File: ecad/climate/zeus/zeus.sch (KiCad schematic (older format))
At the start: 12 parts, among them J1 MCV 1,5/ 2-G-3,5, J10 47053-1000, J11 47053-1000, J12 PT 1,5/4-3,5-H, J13 PT 1,5/4-3,5-H, J2 MCV 1,5/ 2-G-3,5, J3 MCV 1,5/ 2-G-3,5, J5 47053-1000, J6 47053-1000, J7 215079-8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

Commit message: Makes pleiades zeus again
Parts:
- removed J12, J13: PT 1,5/4-3,5-H, TerminalBlock_Phoenix:TerminalBlock_Phoenix_PT-1,5-4-3.5-H_1x04_P3.50mm_Horizontal, symbol Connector_Generic:Conn_01x04
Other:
- moved on the sheet: J3
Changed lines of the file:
@@
 EESchema Schematic File Version 4
-LIBS:pleiades-cache
+LIBS:zeus-cache
 EELAYER 26 0
 EELAYER END
 $Descr A4 11693 8268
 encoding utf-8
-Sheet 1 12
+Sheet 1 10
 Title ""
 Date ""
@@
 L power:+12V #PWR01
 U 1 1 5BA4C0F9
-P 1700 6750
-F 0 "#PWR01" H 1700 6600 50  0001 C CNN
-F 1 "+12V" H 1700 6890 50  0000 C CNN
-F 2 "" H 1700 6750 50  0001 C CNN
-F 3 "" H 1700 6750 50  0001 C CNN
-	1    1700 6750
+P 2200 1250
+F 0 "#PWR01" H 2200 1100 50  0001 C CNN
+F 1 "+12V" H 2200 1390 50  0000 C CNN
+F 2 "" H 2200 1250 50  0001 C CNN
+F 3 "" H 2200 1250 50  0001 C CNN
+	1    2200 1250
 	1    0    0    -1
 $EndComp
@@
 L power:+5V #PWR02
 U 1 1 5BA4C12E
-P 3250 6750
-F 0 "#PWR02" H 3250 6600 50  0001 C CNN
-F 1 "+5V" H 3250 6890 50  0000 C CNN
-F 2 "" H 3250 6750 50  0001 C CNN
-F 3 "" H 3250 6750 50  0001 C CNN
-	1    3250 6750
+P 3750 1250
+F 0 "#PWR02" H 3750 1100 50  0001 C CNN
+F 1 "+5V" H 3750 1390 50  0000 C CNN
+F 2 "" H 3750 1250 50  0001 C CNN
+F 3 "" H 3750 1250 50  0001 C CNN
+	1    3750 1250
 	1    0    0    -1
 $EndComp
@@
 $EndSheet
 $Sheet
-S 3500 6900 1250 200
+S 4000 1400 1250 200
 U 5BA4EFD7
 F0 "3v3 LDO" 60
 F1 "../../common/3V3LDO.sch" 60
-F2 "5V" I L 3500 7000 60
-F3 "3V3" O R 4750 7000 60
-$EndSheet
-$Sheet
-S 1850 6900 1150 200
+F2 "5V" I L 4000 1500 60
+F3 "3V3" O R 5250 1500 60
+$EndSheet
+$Sheet
+S 2350 1400 1150 200
 U 5BA4BC5D
 F0 "5V Buck Converter" 60
 F1 "../../common/12V5VDCDC.sch" 60
-F2 "VIN" I L 1850 7000 60
-F3 "5V" O R 3000 7000 60
+F2 "VIN" I L 2350 1500 60
+F3 "5V" O R 3500 1500 60
 $EndSheet
 $Comp
 L pleiades-rescue:+3.3V #PWR03
 U 1 1 5BA4FC58
-P 4900 6750
-F 0 "#PWR03" H 4900 6600 50  0001 C CNN
-F 1 "+3.3V" H 4900 6890 50  0000 C CNN
-F 2 "" H 4900 6750 50  0001 C CNN
-F 3 "" H 4900 6750 50  0001 C CNN
-	1    4900 6750
+P 5400 1250
+F 0 "#PWR03" H 5400 1100 50  0001 C CNN
+F 1 "+3.3V" H 5400 1390 50  0000 C CNN
+F 2 "" H 5400 1250 50  0001 C CNN
+F 3 "" H 5400 1250 50  0001 C CNN
+	1    5400 1250
 	1    0    0    -1
 $EndComp
@@
 L Connector_Generic:Conn_01x02 J3
 U 1 1 5BA567FD
-P 1050 7000
-F 0 "J3" H 1050 7100 50  0000 C CNN
-F 1 "MCV 1,5/ 2-G-3,5" H 1050 6800 50  0000 C CNN
-F 2 "Connector_Phoenix_MC:PhoenixContact_MCV_1,5_2-G-3.5_1x02_P3.50mm_Vertical" H 1050 7000 50  0001 C CNN
-F 3 "" H 1050 7000 50  0001 C CNN
-F 4 "MCV 1,5/ 2-G-3,5" H 1050 7000 60  0001 C CNN "Part Number"
-	1    1050 7000
+P 1550 1500
+F 0 "J3" H 1550 1600 50  0000 C CNN
+F 1 "MCV 1,5/ 2-G-3,5" H 1550 1300 50  0000 C CNN
+F 2 "Connector_Phoenix_MC:PhoenixContact_MCV_1,5_2-G-3.5_1x02_P3.50mm_Vertical" H 1550 1500 50  0001 C CNN
+F 3 "" H 1550 1500 50  0001 C CNN
+F 4 "MCV 1,5/ 2-G-3,5" H 1550 1500 60  0001 C CNN "Part Number"
+	1    1550 1500
 	-1   0    0    -1
 $EndComp
@@
 L power:GND #PWR08
 U 1 1 5BA570D8
-P 1500 7300
-F 0 "#PWR08" H 1500 7050 50  0001 C CNN
-F 1 "GND" H 1500 7150 50  0000 C CNN
-F 2 "" H 1500 7300 50  0001 C CNN
-F 3 "" H 1500 7300 50  0001 C CNN
-	1    1500 7300
+P 2000 1800
+F 0 "#PWR08" H 2000 1550 50  0001 C CNN
+F 1 "GND" H 2000 1650 50  0000 C CNN
+F 2 "" H 2000 1800 50  0001 C CNN
+F 3 "" H 2000 1800 50  0001 C CNN
+	1    2000 1800
 	1    0    0    -1
 $EndComp
@@
 F7 "SDA_5V" B R 4850 4200 60
 F8 "SCL_5V" O R 4850 4300 60
-F9 "RELAY_1" O R 4850 3500 50
-F10 "RELAY_2" O R 4850 3600 50
 $EndSheet
 $Sheet
@@
 $EndComp
 Wire Wire Line
-	1700 6750 1700 7000
-Wire Wire Line
-	1250 7000 1700 7000
-Wire Wire Line
-	3000 7000 3250 7000
-Wire Wire Line
-	3250 7000 3250 6750
-Connection ~ 3250 7000
-Wire Wire Line
-	4750 7000 4900 7000
-Wire Wire Line
-	4900 7000 4900 6750
+	2200 1250 2200 1500
+Wire Wire Line
+	1750 1500 2200 1500
+Wire Wire Line
+	3500 1500 3750 1500
+Wire Wire Line
+	3750 1500 3750 1250
+Connection ~ 3750 1500
+Wire Wire Line
+	5250 1500 5400 1500
+Wire Wire Line
+	5400 1500 5400 1250
 Wire Wire Line
 	10300 4600 10400 4600
@@
 	1300 4600 900  4600
 Connection ~ 1300 4150
-Connection ~ 1700 7000
-Wire Wire Line
-	1250 7100 1500 7100
-Wire Wire Line
-	1500 7100 1500 7300
+Connection ~ 2200 1500
+Wire Wire Line
+	1750 1600 2000 1600
+Wire Wire Line
+	2000 1600 2000 1800
 Wire Wire Line
 	3400 4050 3600 4050
@@
 	7800 5450 8500 5450
 $Sheet
-S 6100 3650 1250 1250
+S 6100 3550 1250 1300
 U 5BAB6A7C
 F0 "I2C Multiplexer" 60
@@
 F11 "~INT1" I R 7350 4100 60
 F12 "~INT2" I R 7350 4500 60
+F13 "~INT0" I R 7350 3700 50
 $EndSheet
 Wire Wire Line
@@
 	7600 5700 8500 5700
 Wire Wire Line
-	3250 7000 3500 7000
+	3750 1500 4000 1500
 Wire Wire Line
 	10200 4100 10200 4700
@@
 	1300 4150 1550 4150
 Wire Wire Line
-	1700 7000 1850 7000
+	2200 1500 2350 1500
 Wire Wire Line
 	10300 5800 10300 5200
@@
 Wire Wire Line
 	10250 1300 10350 1300
-$Sheet
-S 6100 1100 750  300
-U 5BB4177A
-F0 "Relay 1" 50
-F1 "Relay.sch" 50
-F2 "CMD" I L 6100 1250 50
-F3 "A" B R 6850 1200 50
-F4 "B" B R 6850 1300 50
-$EndSheet
-$Comp
-L Connector_Generic:Conn_01x04 J12
-U 1 1 5BB464E2
-P 7500 1150
-F 0 "J12" H 7579 1142 50  0000 L CNN
-F 1 "PT 1,5/4-3,5-H" H 7579 1051 50  0000 L CNN
-F 2 "TerminalBlock_Phoenix:TerminalBlock_Phoenix_PT-1,5-4-3.5-H_1x04_P3.50mm_Horizontal" H 7500 1150 50  0001 C CNN
-F 3 "~" H 7500 1150 50  0001 C CNN
-F 4 "PT 1,5/4-3,5-H" H 7500 1150 50  0001 C CNN "Part Number"
-	1    7500 1150
-	1    0    0    -1
-$EndComp
-Wire Wire Line
-	7300 1050 7200 1050
-Wire Wire Line
-	7200 1050 7200 1250
-Wire Wire Line
-	7200 1250 7300 1250
-Wire Wire Line
-	6850 1200 7050 1200
-Wire Wire Line
-	7050 1200 7050 1150
-Wire Wire Line
-	7050 1150 7300 1150
-Wire Wire Line
-	6850 1300 7050 1300
-Wire Wire Line
-	7050 1300 7050 1350
-Wire Wire Line
-	7050 1350 7300 1350
-$Sheet
-S 6100 1750 750  300
-U 5BB53554
-F0 "Relay 2" 50
-F1 "Relay.sch" 50
-F2 "CMD" I L 6100 1900 50
-F3 "A" B R 6850 1850 50
-F4 "B" B R 6850 1950 50
-$EndSheet
-$Comp
-L Connector_Generic:Conn_01x04 J13
-U 1 1 5BB5355B
-P 7500 1800
-F 0 "J13" H 7579 1792 50  0000 L CNN
-F 1 "PT 1,5/4-3,5-H" H 7579 1701 50  0000 L CNN
-F 2 "TerminalBlock_Phoenix:TerminalBlock_Phoenix_PT-1,5-4-3.5-H_1x04_P3.50mm_Horizontal" H 7500 1800 50  0001 C CNN
-F 3 "~" H 7500 1800 50  0001 C CNN
-F 4 "PT 1,5/4-3,5-H" H 7500 1800 50  0001 C CNN "Part Number"
-	1    7500 1800
-	1    0    0    -1
-$EndComp
-Wire Wire Line
-	7300 1700 7200 1700
-Wire Wire Line
-	7200 1700 7200 1900
-Wire Wire Line
-	7200 1900 7300 1900
-Wire Wire Line
-	6850 1850 7050 1850
-Wire Wire Line
-	7050 1850 7050 1800
-Wire Wire Line
-	7050 1800 7300 1800
-Wire Wire Line
-	6850 1950 7050 1950
-Wire Wire Line
-	7050 1950 7050 2000
-Wire Wire Line
-	7050 2000 7300 2000
 Wire Wire Line
 	4850 4100 6100 4100
@@
 Wire Wire Line
 	8850 1250 9100 1250
-Wire Wire Line
-	4850 3600 5600 3600
-Wire Wire Line
-	5600 3600 5600 1900
-Wire Wire Line
-	5600 1900 6100 1900
-Wire Wire Line
-	4850 3500 5500 3500
-Wire Wire Line
-	5500 3500 5500 1250
-Wire Wire Line
-	5500 1250 6100 1250
 $EndSCHEMATC

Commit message: Licenses Climate PCB under OHL v1.2
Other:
- note added: "© 2018 Université de Lausanne\n\nThis documentation describes Open Hardware and is licensed under the\nCERN OHL v. 1.2.\n\nYou may redistribute and modify this documentation under the terms of\nthe CERN OHL v.1.2. (http://ohwr.org/cernohl). This documentation is\ndistributed WITHOUT ANY EXPRESS OR IMPLIED WARRANTY,\nINCLUDING OF MERCHANTABILITY, SATISFACTORY QUALITY AND\nFITNESS FOR A PARTICULAR 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"
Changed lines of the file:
@@
 encoding utf-8
 Sheet 1 10
-Title ""
-Date ""
-Rev ""
-Comp ""
-Comment1 ""
-Comment2 ""
+Title "Zeus - Climate Control Board"
+Date "06/11/2018"
+Rev "A"
+Comp "Université de Lausanne"
+Comment1 "Author: Alexandre Tuleu"
+Comment2 "Licensed under the CERN OHL v1.2"
 Comment3 ""
 Comment4 ""
@@
 Wire Wire Line
 	8850 1250 9100 1250
+Text Notes 550  7750 0    50   ~ 0
+© 2018 Université de Lausanne\n\nThis documentation describes Open Hardware and is licensed under the\nCERN OHL v. 1.2.\n\nYou may redistribute and modify this documentation under the terms of\nthe CERN OHL v.1.2. (http://ohwr.org/cernohl). This documentation is\ndistributed WITHOUT ANY EXPRESS OR IMPLIED WARRANTY,\nINCLUDING OF MERCHANTABILITY, SATISFACTORY QUALITY AND\nFITNESS FOR A PARTICULAR PURPOSE. Please see the CERN OHL v.1.2\nfor applicable conditions
 $EndSCHEMATC

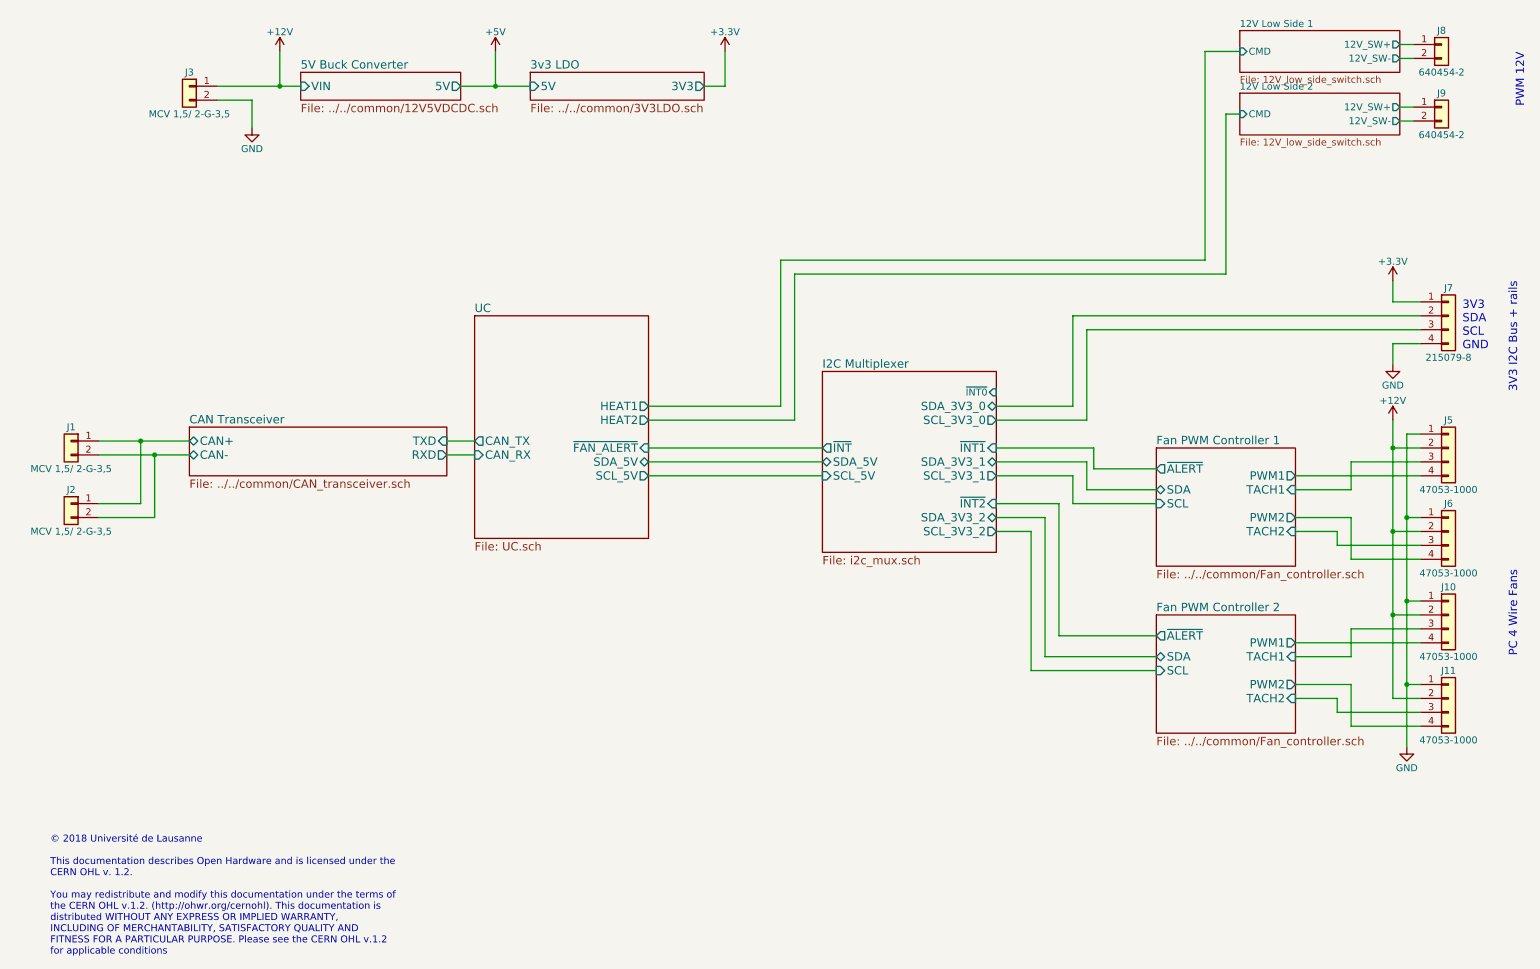
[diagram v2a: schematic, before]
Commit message: Updates climate board to rev B~dev
 * Changes all Power Connectors to MiniFit-JR 5566-02A to avoid
   someone pluging the power supply on the CAN bus as it will destroy
   all MCP2561 on the bus
 * Fixes issues in Arke:
 ** Crossed Rx/Tx lines
 ** Flipped DB9 connector
 * Fixes and Improvment in Celaeno/Zeus:
 ** Added missing pull-up resistor on tachometer inputs
 ** Removed unecessary 32.268kHz oscillators (they are not working
    properly with manual soldering)
 ** Removed I2C multiplexer as we can add a second EMC2302 with a
   different i2c address to do the same thing. Repaced it by an i2c
   level shifter (tested and working).

Many of these changes still need to be tested before going to
production
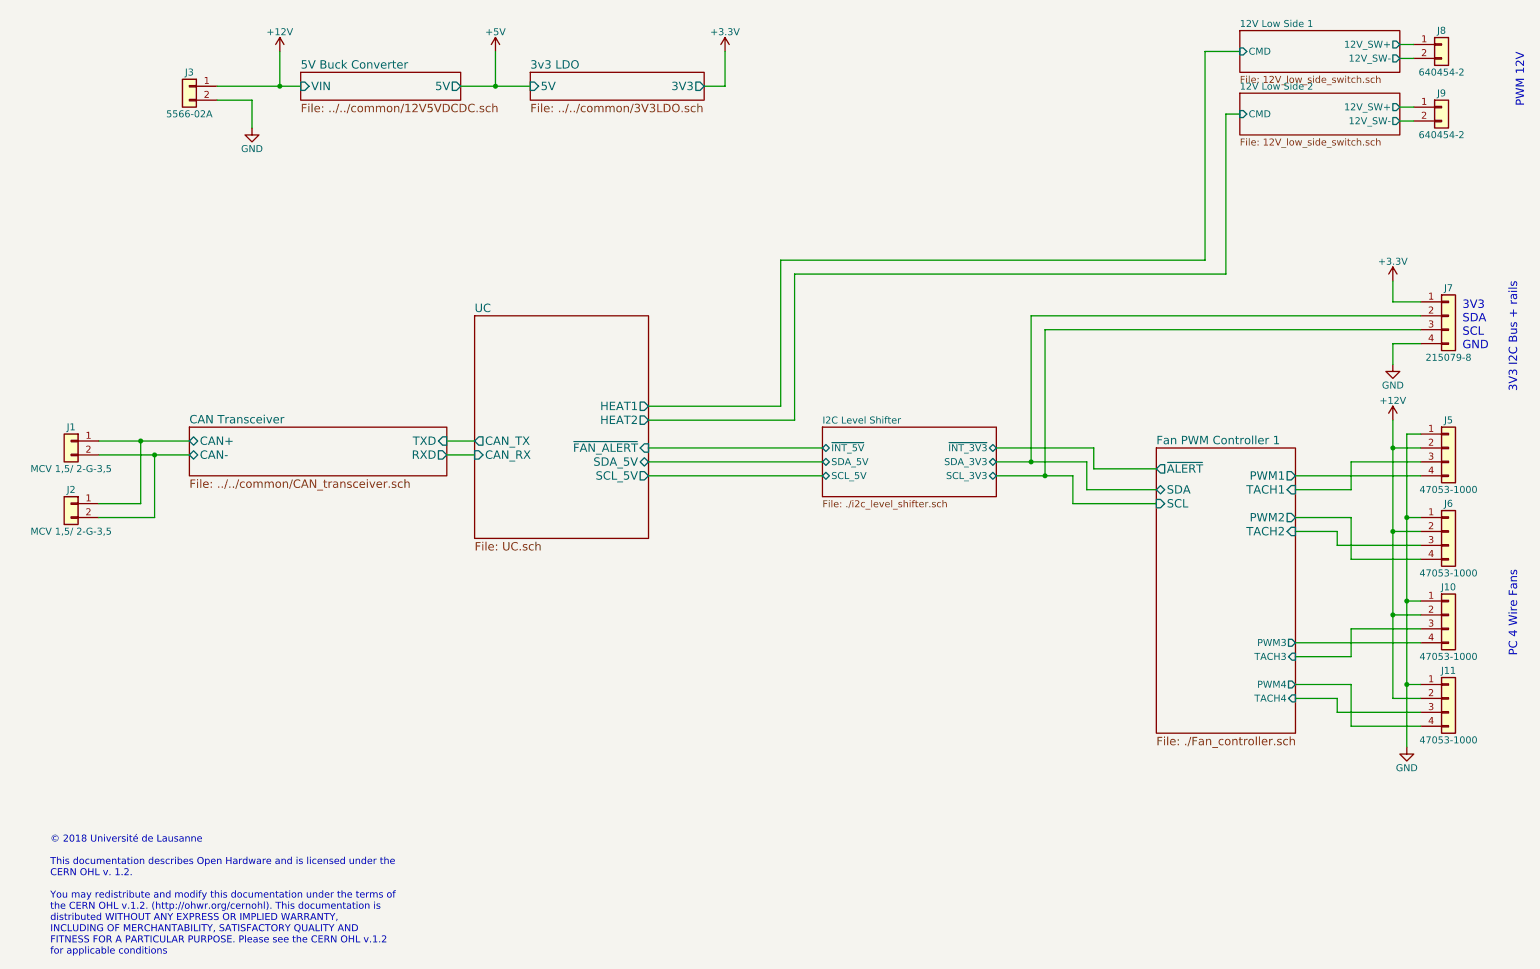
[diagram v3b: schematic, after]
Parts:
- J3: value MCV 1,5/ 2-G-3,5 -> 5566-02A; footprint Connector_Phoenix_MC:PhoenixContact_MCV_1,5_2-G-3.5_1x02_P3.50mm_Vertical -> Connector_Molex:Molex_Mini-Fit_Jr_5566-02A_2x01_P4.20mm_Vertical; Part Number MCV 1,5/ 2-G-3,5 -> 39-28-1023
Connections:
- net I2C Multiplexer/SCL_3V3_0 is gone; now on net Fan PWM Controller 1/SCL: J7.3 (Pin_3)
- net I2C Multiplexer/SDA_3V3_0 is gone; now on net Fan PWM Controller 1/SDA: J7.2 (Pin_2)
- net Fan PWM Controller 2/PWM1 renamed Fan PWM Controller 1/PWM3
- net Fan PWM Controller 2/PWM2 renamed Fan PWM Controller 1/PWM4
- net Fan PWM Controller 2/TACH1 renamed Fan PWM Controller 1/TACH3
- net Fan PWM Controller 2/TACH2 renamed Fan PWM Controller 1/TACH4
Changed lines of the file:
@@
 $Descr A4 11693 8268
 encoding utf-8
-Sheet 1 10
+Sheet 1 9
 Title "Zeus - Climate Control Board"
 Date "06/11/2018"
-Rev "A"
+Rev "B"
 Comp "Université de Lausanne"
 Comment1 "Author: Alexandre Tuleu"
@@
 $EndComp
 $Sheet
-S 8500 4100 1000 850
+S 8500 4100 1000 2050
 U 5BA5AC9B
 F0 "Fan PWM Controller 1" 60
-F1 "../../common/Fan_controller.sch" 60
+F1 "./Fan_controller.sch" 60
 F2 "PWM1" O R 9500 4300 60
 F3 "PWM2" O R 9500 4600 60
@@
 F7 "SDA" B L 8500 4400 60
 F8 "SCL" I L 8500 4500 60
+F9 "PWM3" O R 9500 5500 50
+F10 "PWM4" O R 9500 5800 50
+F11 "TACH3" I R 9500 5600 50
+F12 "TACH4" I R 9500 5900 50
 $EndSheet
 $Comp
@@
 P 1550 1500
 F 0 "J3" H 1550 1600 50  0000 C CNN
-F 1 "MCV 1,5/ 2-G-3,5" H 1550 1300 50  0000 C CNN
-F 2 "Connector_Phoenix_MC:PhoenixContact_MCV_1,5_2-G-3.5_1x02_P3.50mm_Vertical" H 1550 1500 50  0001 C CNN
+F 1 "5566-02A" H 1550 1300 50  0000 C CNN
+F 2 "Connector_Molex:Molex_Mini-Fit_Jr_5566-02A_2x01_P4.20mm_Vertical" H 1550 1500 50  0001 C CNN
 F 3 "" H 1550 1500 50  0001 C CNN
-F 4 "MCV 1,5/ 2-G-3,5" H 1550 1500 60  0001 C CNN "Part Number"
+F 4 "39-28-1023" H 1550 1500 60  0001 C CNN "Part Number"
 	1    1550 1500
 	-1   0    0    -1
@@
 F8 "SCL_5V" O R 4850 4300 60
 $EndSheet
-$Sheet
-S 8500 5300 1000 850
-U 5BAA713E
-F0 "Fan PWM Controller 2" 60
-F1 "../../common/Fan_controller.sch" 60
-F2 "PWM1" O R 9500 5500 60
-F3 "PWM2" O R 9500 5800 60
-F4 "TACH1" I R 9500 5600 60
-F5 "TACH2" I R 9500 5900 60
-F6 "~ALERT" O L 8500 5450 60
-F7 "SDA" B L 8500 5600 60
-F8 "SCL" I L 8500 5700 60
-$EndSheet
 $Comp
 L Connector_Generic:Conn_01x04 J10
@@
 	8050 4250 8500 4250
 Wire Wire Line
-	7800 5450 8500 5450
-$Sheet
-S 6100 3550 1250 1300
-U 5BAB6A7C
-F0 "I2C Multiplexer" 60
-F1 "i2c_mux.sch" 60
-F2 "~INT" O L 6100 4100 60
-F3 "SCL_5V" I L 6100 4300 60
-F4 "SDA_5V" B L 6100 4200 60
-F5 "SCL_3V3_0" O R 7350 3900 60
-F6 "SCL_3V3_1" O R 7350 4300 60
-F7 "SCL_3V3_2" O R 7350 4700 60
-F8 "SDA_3V3_0" B R 7350 3800 60
-F9 "SDA_3V3_1" B R 7350 4200 60
-F10 "SDA_3V3_2" B R 7350 4600 60
-F11 "~INT1" I R 7350 4100 60
-F12 "~INT2" I R 7350 4500 60
-F13 "~INT0" I R 7350 3700 50
-$EndSheet
-Wire Wire Line
-	7350 3800 7900 3800
-Wire Wire Line
-	7900 3800 7900 3150
-Wire Wire Line
-	7900 3150 10400 3150
-Wire Wire Line
-	10400 3250 8000 3250
-Wire Wire Line
-	8000 3250 8000 3900
-Wire Wire Line
-	8000 3900 7350 3900
-Wire Wire Line
 	7350 4100 8050 4100
 Wire Wire Line
 	8050 4100 8050 4250
 Wire Wire Line
-	7350 4200 8000 4200
+	7350 4200 7600 4200
 Wire Wire Line
 	8000 4200 8000 4400
@@
 	8000 4400 8500 4400
 Wire Wire Line
-	7350 4300 7900 4300
+	7350 4300 7700 4300
 Wire Wire Line
 	7900 4300 7900 4500
 Wire Wire Line
 	7900 4500 8500 4500
-Wire Wire Line
-	7350 4500 7800 4500
-Wire Wire Line
-	7800 4500 7800 5450
-Wire Wire Line
-	7350 4600 7700 4600
-Wire Wire Line
-	7700 4600 7700 5600
-Wire Wire Line
-	7700 5600 8500 5600
-Wire Wire Line
-	7350 4700 7600 4700
-Wire Wire Line
-	7600 4700 7600 5700
-Wire Wire Line
-	7600 5700 8500 5700
 Wire Wire Line
 	3750 1500 4000 1500
@@
 Text Notes 550  7750 0    50   ~ 0
 © 2018 Université de Lausanne\n\nThis documentation describes Open Hardware and is licensed under the\nCERN OHL v. 1.2.\n\nYou may redistribute and modify this documentation under the terms of\nthe CERN OHL v.1.2. (http://ohwr.org/cernohl). This documentation is\ndistributed WITHOUT ANY EXPRESS OR IMPLIED WARRANTY,\nINCLUDING OF MERCHANTABILITY, SATISFACTORY QUALITY AND\nFITNESS FOR A PARTICULAR PURPOSE. Please see the CERN OHL v.1.2\nfor applicable conditions
+$Sheet
+S 6100 3950 1250 500
+U 5BEDDB19
+F0 "I2C Level Shifter" 50
+F1 "./i2c_level_shifter.sch" 50
+F2 "SDA_5V" B L 6100 4200 50
+F3 "SCL_5V" B L 6100 4300 50
+F4 "SDA_3V3" B R 7350 4200 50
+F5 "SCL_3V3" B R 7350 4300 50
+F6 "~INT_3V3" B R 7350 4100 50
+F7 "~INT_5V" B L 6100 4100 50
+$EndSheet
+Wire Wire Line
+	7600 3150 7600 4200
+Wire Wire Line
+	7600 3150 10400 3150
+Connection ~ 7600 4200
+Wire Wire Line
+	7600 4200 8000 4200
+Wire Wire Line
+	7700 3250 7700 4300
+Wire Wire Line
+	7700 3250 10400 3250
+Connection ~ 7700 4300
+Wire Wire Line
+	7700 4300 7900 4300
 $EndSCHEMATC

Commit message: Adds TVS on Zeus I2C bus
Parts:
- added D11: CPDT-5V0USP-HF, Package_TO_SOT_SMD:SOT-23, symbol Device:D_TVS_x2_AAC
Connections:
- net Fan PWM Controller 1/SCL: now also D11.2 (A2)
- net Fan PWM Controller 1/SDA: now also D11.1 (A1)
- net GND: now also D11.3 (common)
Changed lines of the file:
@@
 	7600 3150 7600 4200
 Wire Wire Line
-	7600 3150 10400 3150
+	7600 3150 9900 3150
 Connection ~ 7600 4200
 Wire Wire Line
@@
 	7700 3250 7700 4300
 Wire Wire Line
-	7700 3250 10400 3250
+	7700 3250 9000 3250
 Connection ~ 7700 4300
 Wire Wire Line
 	7700 4300 7900 4300
+$Comp
+L Device:D_TVS_x2_AAC D11
+U 1 1 5BFFE99E
+P 9450 3500
+F 0 "D11" H 9450 3716 50  0000 C CNN
+F 1 "CPDT-5V0USP-HF" H 9450 3625 50  0000 C CNN
+F 2 "Package_TO_SOT_SMD:SOT-23" H 9300 3500 50  0001 C CNN
+F 3 "~" H 9300 3500 50  0001 C CNN
+F 4 "CPDT-5V0USP-HF" H 9450 3500 50  0001 C CNN "Part Number"
+	1    9450 3500
+	-1   0    0    -1
+$EndComp
+Wire Wire Line
+	9100 3500 9000 3500
+Wire Wire Line
+	9000 3500 9000 3250
+Connection ~ 9000 3250
+Wire Wire Line
+	9000 3250 10400 3250
+Wire Wire Line
+	9800 3500 9900 3500
+Wire Wire Line
+	9900 3500 9900 3150
+Connection ~ 9900 3150
+Wire Wire Line
+	9900 3150 10400 3150
+$Comp
+L power:GND #PWR0101
+U 1 1 5C0042E3
+P 9450 3750
+F 0 "#PWR0101" H 9450 3500 50  0001 C CNN
+F 1 "GND" H 9455 3577 50  0000 C CNN
+F 2 "" H 9450 3750 50  0001 C CNN
+F 3 "" H 9450 3750 50  0001 C CNN
+	1    9450 3750
+	1    0    0    -1
+$EndComp
+Wire Wire Line
+	9450 3750 9450 3650
 $EndSCHEMATC

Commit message: Makes all electronics production ready
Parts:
- J3: footprint Connector_Molex:Molex_Mini-Fit_Jr_5566-02A_2x01_P4.20mm_Vertical -> FORT:Molex_Mini-Fit_Jr_5566-02A_2x01_P4.20mm_Vertical
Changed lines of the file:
@@
 F 0 "J3" H 1550 1600 50  0000 C CNN
 F 1 "5566-02A" H 1550 1300 50  0000 C CNN
-F 2 "Connector_Molex:Molex_Mini-Fit_Jr_5566-02A_2x01_P4.20mm_Vertical" H 1550 1500 50  0001 C CNN
+F 2 "FORT:Molex_Mini-Fit_Jr_5566-02A_2x01_P4.20mm_Vertical" H 1550 1500 50  0001 C CNN
 F 3 "" H 1550 1500 50  0001 C CNN
 F 4 "39-28-1023" H 1550 1500 60  0001 C CNN "Part Number"
